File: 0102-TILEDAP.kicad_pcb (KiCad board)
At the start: 4 copper layers, 42.1 x 24.6 mm, 40 parts, among them J1 USB-C, J2 IF, J3 TGT, SW1 SW_Push, U1 SPX3819M5-L-3-3, U2 STM32F103TBUx, Y1 8MHz

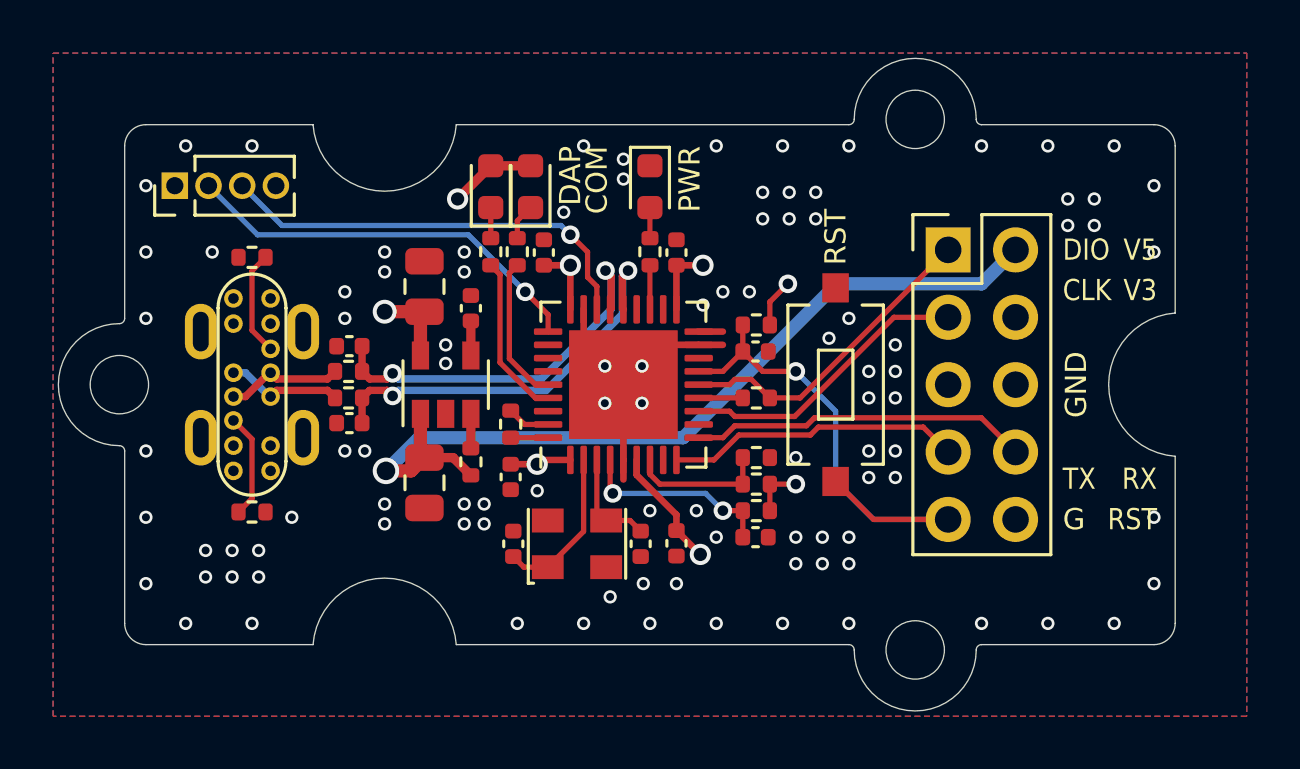
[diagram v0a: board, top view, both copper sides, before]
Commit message: Fix USB enumerate
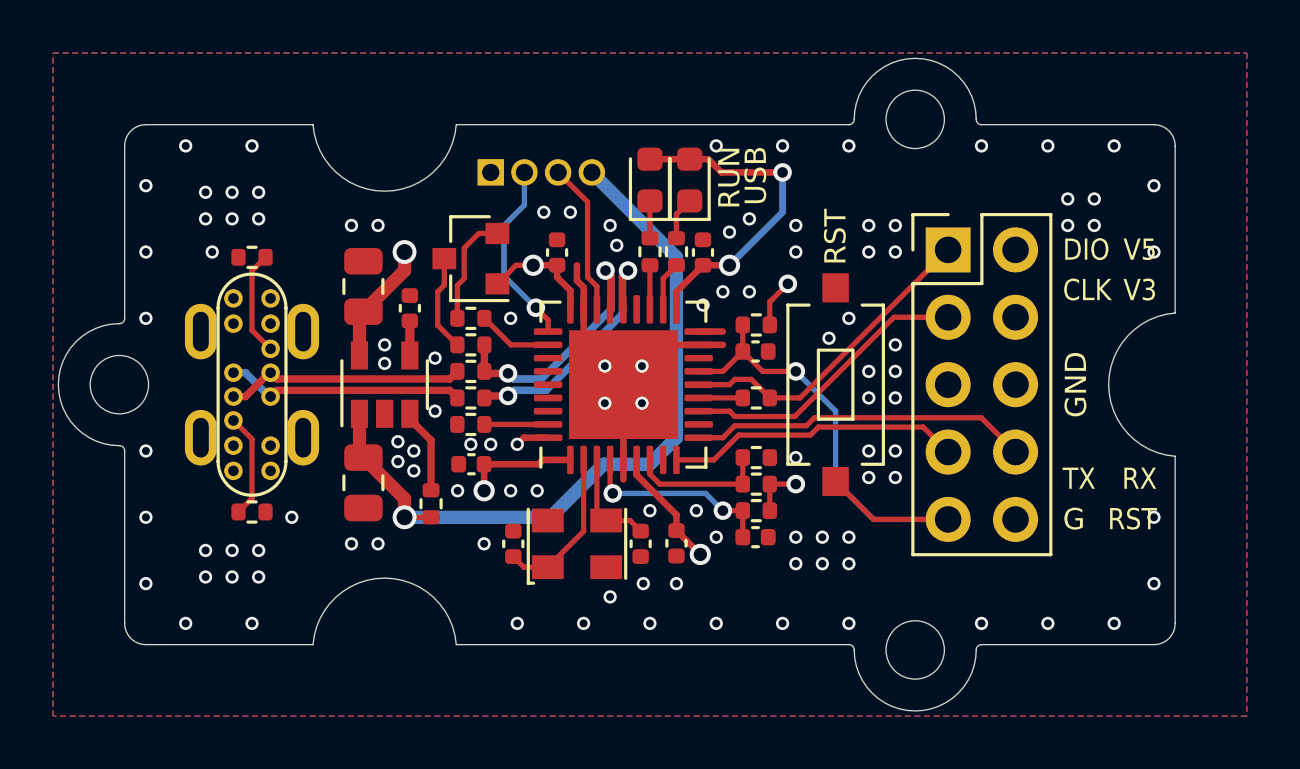
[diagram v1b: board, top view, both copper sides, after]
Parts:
- removed C10, C9: 18pF, Capacitor_SMD:C_0402_1005Metric
- removed D2: GRN, LED_SMD:LED_0603_1608Metric
- added Q1: S8550, Package_TO_SOT_SMD:SOT-23, F.Cu at (113.2, 105.2)
- added R10: 1.5K, Resistor_SMD:R_0402_1005Metric, F.Cu at (113.2, 108.5)
- J2: moved to B.Cu
- R4, R5: value 33R -> 0R
- moved J2 11.9 mm to (114.0, 102.0), turned to 270 degrees
- moved D1 7.50 mm to (121.5, 102.3)
- moved R11 7.00 mm to (121.0, 105.0)
- moved R4 4.61 mm to (113.2, 110.5)
- moved R5 4.61 mm to (113.2, 109.5)
- moved R14 3.06 mm to (113.2, 107.5), turned to 180 degrees
- moved C1 2.30 mm to (109.2, 113.7)
- moved C2 2.30 mm to (111.0, 107.1)
- moved C3 2.30 mm to (109.2, 106.3)
- moved U1 2.30 mm to (110.0, 110.0)
- moved R2 2.18 mm to (111.8, 114.5)
- moved C6 1.56 mm to (113.3, 113.0), turned to 0 degrees
- moved R8 1.50 mm to (113.2, 111.5), turned to 180 degrees
- moved C5 1.00 mm to (122.0, 105.0)
- moved C7 0.50 mm to (116.5, 105.0)
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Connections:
- net /LED_PWR_RED renamed /LED_RUN_RED
- D3 pad 1: GND -> Net-(D3-Pad1)
- D3 pad 2: Net-(D3-Pad2) -> +3V3
- J1 pad S1: Net-(J1-PadS1) -> GND
- J3 pad 7: /TGT_RX -> /TGT_TX
- J3 pad 8: /TGT_TX -> /TGT_RX
- R11 pad 1: /LED_DAP_BLUE -> /LED_CON_BLUE
- R14 pad 1: /LED_COM_GRN -> /USB_ENUM
- R15 pad 2: Net-(D3-Pad2) -> Net-(D3-Pad1)
- U2 pad 10: /TGT_TX -> /TGT_RX
- U2 pad 20: (no net) -> /LED_CON_BLUE
- U2 pad 29: (no net) -> /USB_ENUM
- U2 pad 32: /LED_COM_GRN -> (no net)
- U2 pad 33: /LED_DAP_BLUE -> (no net)
- U2 pad 9: /TGT_RX -> /TGT_TX
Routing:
- net /IF_SWDIO: track 16.4 -> 5.77 mm, vias 1 -> 0
- net VBUS: track 38.2 -> 48.6 mm
- net /IF_SWCLK: track 15.5 -> 7.01 mm
- net +3V3: track 76.5 -> 83.3 mm
- net /LED_DAP_BLUE: track 6.18 -> 0.00 mm
- net /TGT_USB_D-: track 15.5 -> 9.80 mm
- net /LED_COM_GRN: track 5.51 -> 0.00 mm
- net /TGT_USB_D+: track 14.8 -> 10.1 mm
- net /D-: track 4.42 -> 9.03 mm
- net /D+: track 4.42 -> 9.03 mm
- net Net-(Q1-Pad3): track 0.00 -> 3.66 mm
- net Net-(Q1-Pad2): track 1.36 -> 4.24 mm
- net /USB_ENUM: track 0.00 -> 2.82 mm
- net /LED_CON_BLUE: track 0.00 -> 1.87 mm
- net Net-(R2-Pad1): track 1.30 -> 3.01 mm
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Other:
- board text added: "#0102 DAPLink V1.1"
- board text added: "RUN"
- board text added: "USB"
- board text removed: "#0102 DAPLink V1.0"
- board text removed: "COM"
- board text removed: "DAP"
- board text removed: "PWR"

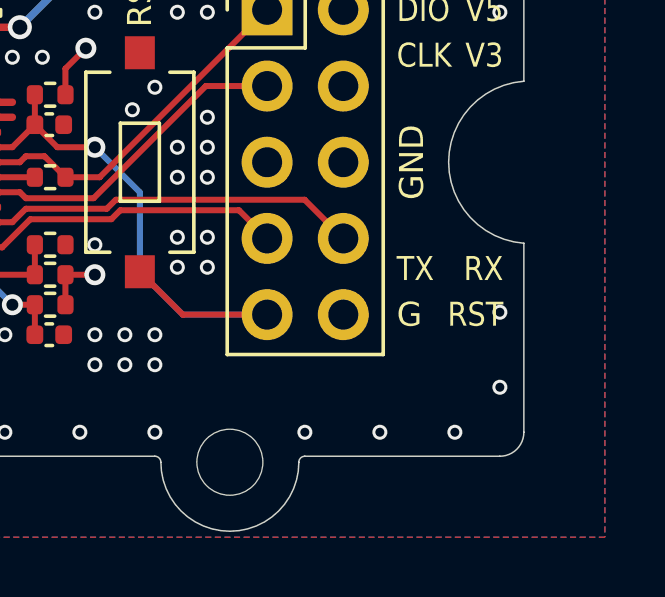
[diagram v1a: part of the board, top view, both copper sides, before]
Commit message: Correct silks
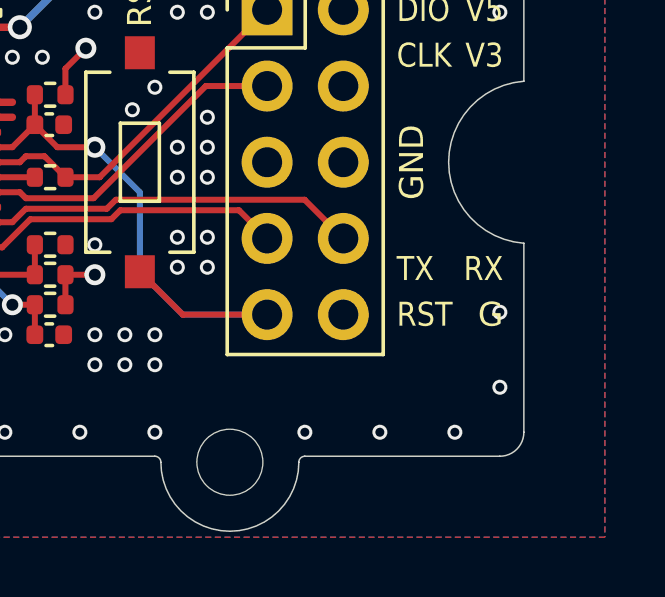
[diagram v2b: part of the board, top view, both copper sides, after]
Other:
- board text added: "#0102 TILEDAP V1.1"
- board text removed: "#0102 DAPLink V1.1"
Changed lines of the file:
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@@
   )
   (page A4)
+  (title_block
+    (title "#0102 TILEDAP")
+    (date 2022-09-07)
+    (rev V1.1)
+  )
   (layers
     (0 F.Cu signal)
@@
     (effects (font (size 0.8 0.8) (thickness 0.12)) (justify left mirror))
   )
-  (gr_text "#0102 DAPLink\nV1.1" (at 113 110 180) (layer B.SilkS)
+  (gr_text "#0102 TILEDAP\nV1.1" (at 113 110 180) (layer B.SilkS)
     (effects (font (size 1 1) (thickness 0.15)) (justify left mirror))
   )
@@
     (effects (font (size 0.8 0.8) (thickness 0.12)))
   )
-  (gr_text G (at 135.56 115.08) (layer F.SilkS)
-    (effects (font (size 0.8 0.8) (thickness 0.12)) (justify left))
-  )
-  (gr_text RST (at 139.116 115.08) (layer F.SilkS)
-    (effects (font (size 0.8 0.7) (thickness 0.12)) (justify right))
+  (gr_text RST (at 135.56 115.08) (layer F.SilkS)
+    (effects (font (size 0.8 0.7) (thickness 0.12)) (justify left))
+  )
+  (gr_text G (at 139.116 115.08) (layer F.SilkS)
+    (effects (font (size 0.8 0.8) (thickness 0.12)) (justify right))
   )
   (gr_text TX (at 135.56 113.556) (layer F.SilkS)

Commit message: Output gerber V1.1
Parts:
- U2: value STM32F103TBUx -> STM32F103TBU6
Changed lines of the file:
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@@
       (effects (font (size 1 1) (thickness 0.15)))
     )
-    (fp_text value STM32F103TBUx (at 0 4.32 90) (layer F.Fab)
+    (fp_text value STM32F103TBU6 (at 0 4.32 90) (layer F.Fab)
       (effects (font (size 1 1) (thickness 0.15)))
     )

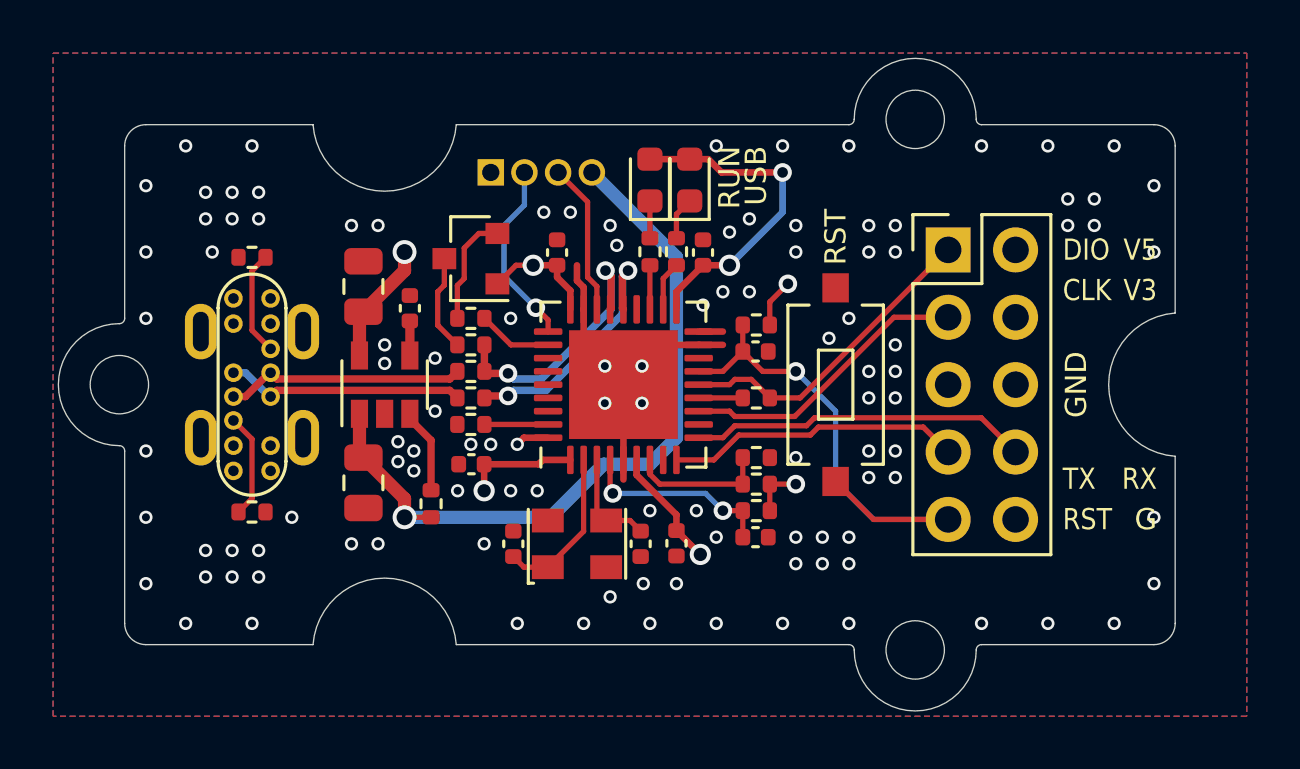
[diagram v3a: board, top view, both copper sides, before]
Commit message: Migrate to KiCad 6
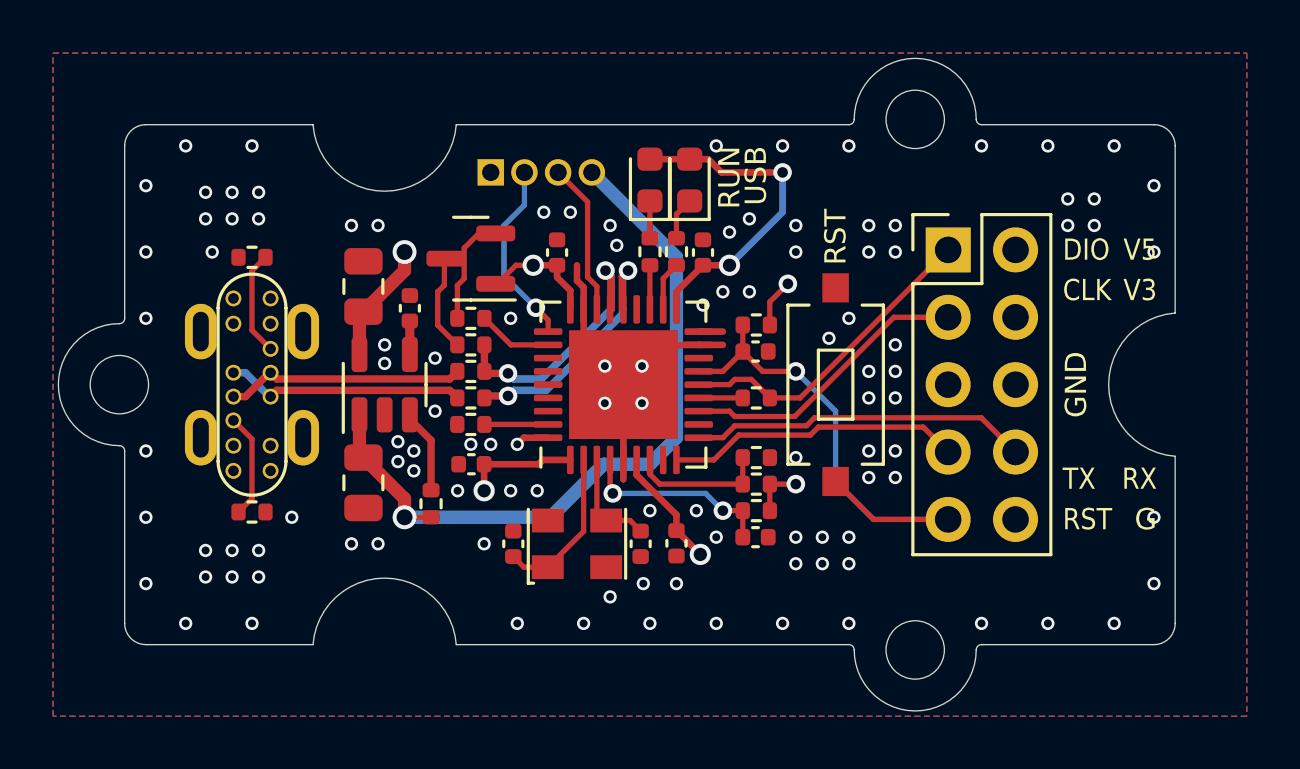
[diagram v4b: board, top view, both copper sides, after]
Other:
- net class Default removed
- net class RF removed
- net class VCC removed

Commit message: Rework silks
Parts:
- added kibuzzard-631DCF04: G***, kibuzzard-631DCF04, F.Cu at (137.4, 106.4)
- added kibuzzard-631DCF09: G***, kibuzzard-631DCF09, F.Cu at (137.4, 104.9)
- added kibuzzard-631DCF21: G***, kibuzzard-631DCF21, F.Cu at (136.0, 110.0)
- added kibuzzard-631DCF2A: G***, kibuzzard-631DCF2A, F.Cu at (137.4, 113.6)
- added kibuzzard-631DCF4E: G***, kibuzzard-631DCF4E, F.Cu at (137.4, 115.1)
- added kibuzzard-631DD701: G***, kibuzzard-631DD701, F.Cu at (127.0, 104.0)
- added kibuzzard-631DD707: G***, kibuzzard-631DD707, F.Cu at (121.4, 102.3)
- added kibuzzard-631DD70B: G***, kibuzzard-631DD70B, F.Cu at (124.4, 102.3)
- added kibuzzard-631DDA4D: G***, kibuzzard-631DDA4D, F.Cu at (103.5, 101.5)
- added kibuzzard-631EEA50: G***, kibuzzard-631EEA50, F.Cu at (102.5, 118.5)
- moved D1 1.50 mm to (123.0, 102.3)
- moved C2 0.19 mm to (110.8, 107.0)
- moved C1 0.10 mm to (109.2, 113.8)
- moved C3 0.10 mm to (109.2, 106.2)
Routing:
- net GND: track 15.3 -> 17.5 mm, vias 110 -> 90
- net +3V3: track 83.3 -> 82.0 mm
- net Net-(D1-Pad1): track 1.61 -> 2.58 mm
- net /D-: vias 0 -> 1
- net /D+: vias 0 -> 1
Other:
- board text added: "TILEDAP"
- board text removed: "#0102 TILEDAP V1.1"
- board text removed: "CLK"
- board text removed: "DIO"
- board text removed: "G"
- board text removed: "RST"
- board text removed: "RUN"
- board text removed: "RX"
- board text removed: "TX"
- board text removed: "USB"
- board text removed: "V3"
- board text removed: "V5"
